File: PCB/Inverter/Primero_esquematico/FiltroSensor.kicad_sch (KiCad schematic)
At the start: 5 parts

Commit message: Termine el circuito de corriente
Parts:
- added C80: 2.2nF, symbol Device:C
- added C82, C83, C84: 300pF, symbol Device:C
- added R142, R143, R144: 100, symbol Device:R
- added R145, R146, R153: 5k1, symbol Device:R
- added U2: TLV9004QDRQ1, Package_SO:SOIC-14_3.9x8.7mm_P1.27mm, symbol Amplifier_Operational:TLV9004xRUCR
- C78: value 1nF -> 2.2nF
- C79: value 10n -> 2.2nF
- R138: value 15k -> 10k
- R139: value 51 -> 10k
- R140: value 100 -> 10k
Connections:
- net GND: now also R139.2, C80.1, C82.1, C83.1, C84.1, U2.10 (V-)
- removed net Sensor_In: C78.2, R138.1, R139.1
- removed net Sensor_Out: C79.2, R139.2, R140.1
- new net: R143.2, U2.5 (-), U2.6
- new net: R144.2, U2.7, U2.8 (-)
- new net: R142.2, U2.1 (-), U2.14
- new net: R140.1, R153.1, U2.9 (+)
- new net: R138.1, R145.1, U2.2 (+)
- new net: R139.1, R146.1, U2.4 (+)
- new net +3.3V: U2.3 (V+)
- new net Sensor_In_1: C78.2, R145.2
- new net Sensor_In_2: C79.2, R146.2
- new net Sensor_In_3: C80.2, R153.2
- new net Sensor_Out_1: C82.2, R142.1
- new net Sensor_Out_2: C83.2, R143.1
- new net Sensor_Out_3: C84.2, R144.1
- no-connect marks 0 -> 3
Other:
- note added: "CL<2.2 nF Rl>10k Ohms"
- moved on the sheet: C78, R138

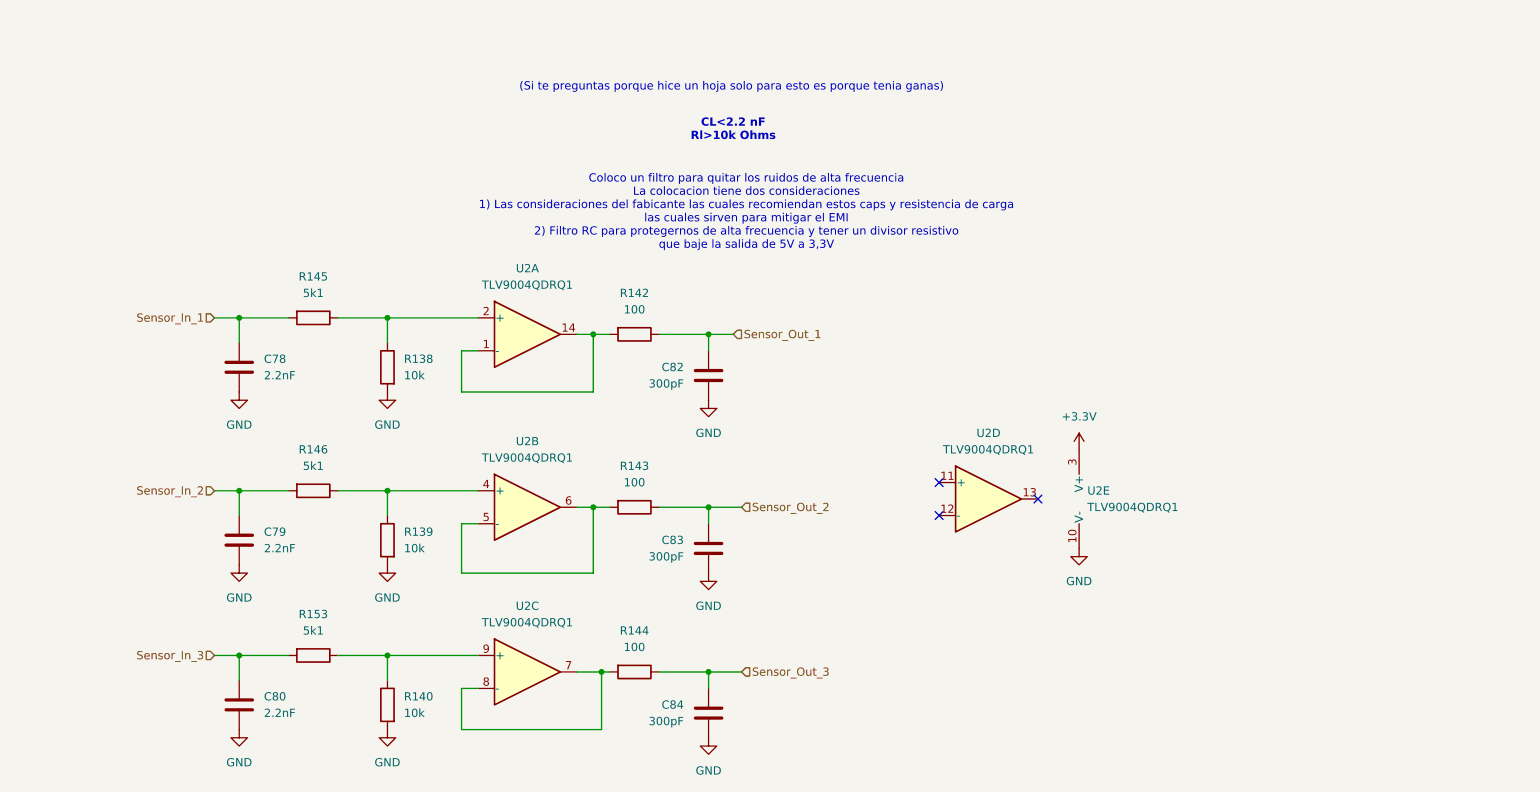
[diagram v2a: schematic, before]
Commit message: Coloque filtros y sensores
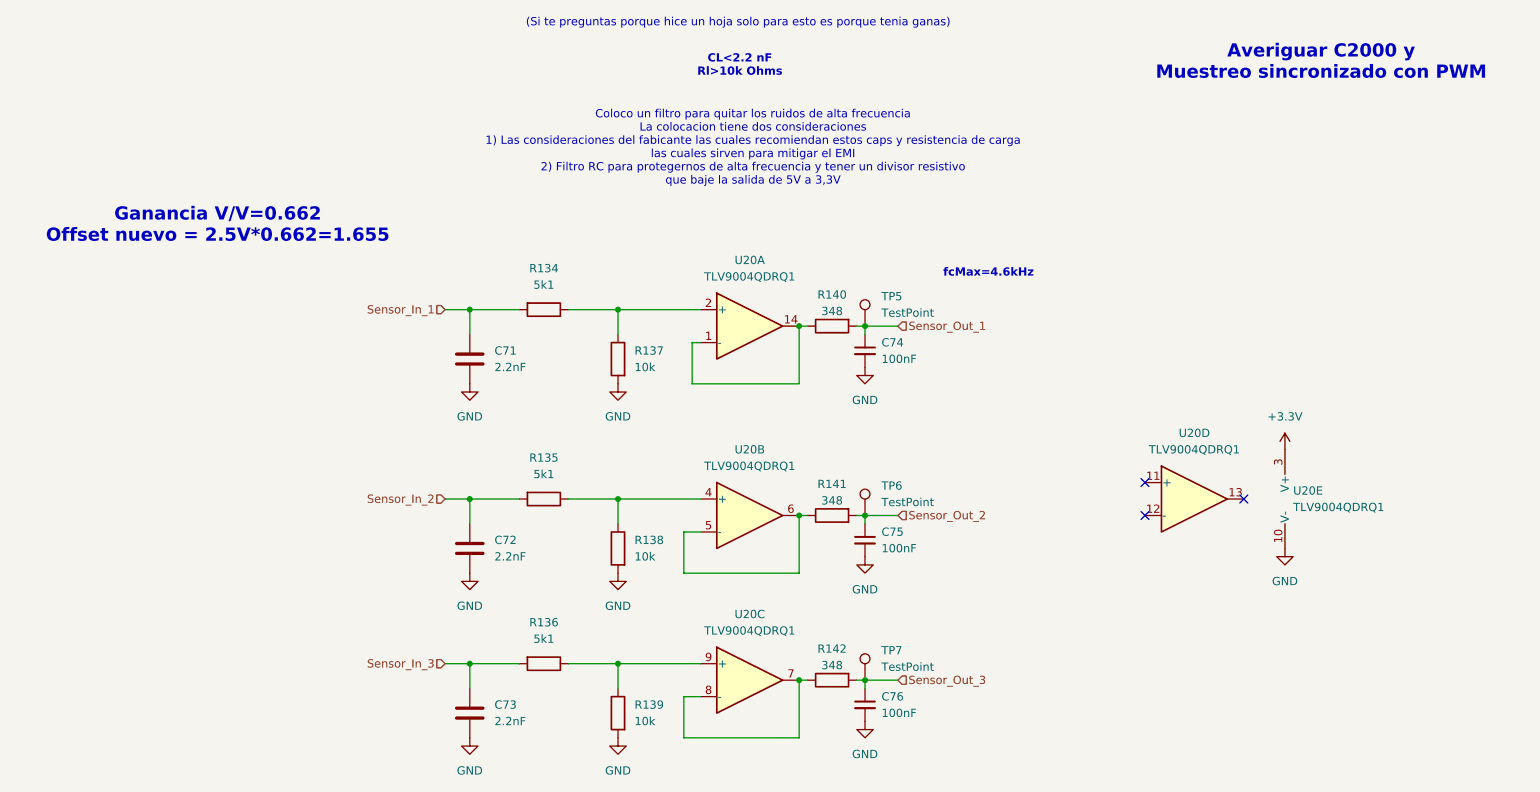
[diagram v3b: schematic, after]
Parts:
- removed C82, C83, C84: 300pF, symbol Device:C
- removed R143, R144: 100, symbol Device:R
- added C74, C75, C76: 100nF, symbol Device:C_Small
- added R140, R141: 348, symbol Device:R
- added TP5, TP6, TP7: TestPoint, symbol Connector:TestPoint
- R142: value 100 -> 348
- renumbered C78 to C71, C79 to C72, C80 to C73, R145 to R134, R146 to R135, R153 to R136, R138 to R137, R139 to R138, R140 to R139, U2 to U20
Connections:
- net GND: now also C74.2, C75.2, C76.2
- net Sensor_Out_1: now also C74.1, R140.2, TP5.1; no longer R142.1
- net Sensor_Out_2: now also C75.1, R141.2, TP6.1
- net Sensor_Out_3: now also R142.2, C76.1, TP7.1
- net at U20.5 (-), U20.6: now also R141.1
- net at U20.7, U20.8 (-): now also R142.1
- net at U20.1 (-), U20.14: now also R140.1; no longer R142.2
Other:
- note added: "Averiguar C2000 y Muestreo sincronizado con PWM"
- note added: "Ganancia V/V=0.662 Offset nuevo = 2.5V*0.662=1.655"
- note added: "fcMax=4.6kHz"
- moved on the sheet: C71, C72, C73, R134, R135, R136, R137, R138, R139, U20A, U20B, U20C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

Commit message: Esquematico practicamente terminado
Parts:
- C71, C72, C73, C74, C75, C76: footprint (none) -> Capacitor_SMD:C_0603_1608Metric
- R134, R135, R136, R137, R138, R139, R140, R141, R142: footprint (none) -> Resistor_SMD:R_0402_1005Metric
- TP5, TP6, TP7: footprint (none) -> TestPoint:TestPoint_Pad_D2.0mm
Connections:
- net +3.3V renamed +3.3VA
- net GND renamed GND1

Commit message: Un par de cosas q corregi del ERC pero sigue mal
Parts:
- U20: footprint Package_SO:SOIC-14_3.9x8.7mm_P1.27mm -> Package_DFN_QFN:Texas_S-PX2QFN-14
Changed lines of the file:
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@@
 			)
 		)
-		(property "Description" "-- valores mixtos --"
+		(property "Description" "Resistor"
 			(at 129.54 133.35 0)
 			(hide yes)
@@
 			)
 		)
-		(property "Description" "-- valores mixtos --"
+		(property "Description" "Resistor"
 			(at 129.54 78.74 0)
 			(hide yes)
@@
 			)
 		)
-		(property "Description" "-- valores mixtos --"
+		(property "Description" "Resistor"
 			(at 129.54 107.95 0)
 			(hide yes)
@@
 			)
 		)
-		(property "Footprint" "Package_SO:SOIC-14_3.9x8.7mm_P1.27mm"
+		(property "Footprint" "Package_DFN_QFN:Texas_S-PX2QFN-14"
 			(at 149.86 73.66 0)
 			(hide yes)
@@
 			)
 		)
-		(property "Datasheet" "https://www.ti.com/lit/ds/symlink/tlv9002-q1.pdf"
+		(property "Datasheet" "http://www.ti.com/lit/ds/symlink/tlv9004.pdf"
 			(at 151.13 68.58 0)
 			(hide yes)
@@
 			)
 		)
-		(property "Description" "-- valores mixtos --"
+		(property "Description" "Low-Power, Quad-Operational Amplifiers, Texas S-PX2QFN-14"
 			(at 149.86 73.66 0)
 			(hide yes)
@@
 			)
 		)
-		(property "Footprint" "Package_SO:SOIC-14_3.9x8.7mm_P1.27mm"
+		(property "Footprint" "Package_DFN_QFN:Texas_S-PX2QFN-14"
 			(at 149.86 102.87 0)
 			(hide yes)
@@
 			)
 		)
-		(property "Datasheet" "https://www.ti.com/lit/ds/symlink/tlv9002-q1.pdf"
+		(property "Datasheet" "http://www.ti.com/lit/ds/symlink/tlv9004.pdf"
 			(at 151.13 97.79 0)
 			(hide yes)
@@
 			)
 		)
-		(property "Description" "-- valores mixtos --"
+		(property "Description" "Low-Power, Quad-Operational Amplifiers, Texas S-PX2QFN-14"
 			(at 149.86 102.87 0)
 			(hide yes)
@@
 			)
 		)
-		(property "Footprint" "Package_SO:SOIC-14_3.9x8.7mm_P1.27mm"
+		(property "Footprint" "Package_DFN_QFN:Texas_S-PX2QFN-14"
 			(at 149.86 128.27 0)
 			(hide yes)
@@
 			)
 		)
-		(property "Datasheet" "https://www.ti.com/lit/ds/symlink/tlv9002-q1.pdf"
+		(property "Datasheet" "http://www.ti.com/lit/ds/symlink/tlv9004.pdf"
 			(at 151.13 123.19 0)
 			(hide yes)
@@
 			)
 		)
-		(property "Description" "-- valores mixtos --"
+		(property "Description" "Low-Power, Quad-Operational Amplifiers, Texas S-PX2QFN-14"
 			(at 149.86 128.27 0)
 			(hide yes)
@@
 			)
 		)
-		(property "Footprint" "Package_SO:SOIC-14_3.9x8.7mm_P1.27mm"
+		(property "Footprint" "Package_DFN_QFN:Texas_S-PX2QFN-14"
 			(at 234.95 100.33 0)
 			(hide yes)
@@
 			)
 		)
-		(property "Datasheet" "https://www.ti.com/lit/ds/symlink/tlv9002-q1.pdf"
+		(property "Datasheet" "http://www.ti.com/lit/ds/symlink/tlv9004.pdf"
 			(at 236.22 95.25 0)
 			(hide yes)
@@
 			)
 		)
-		(property "Description" "-- valores mixtos --"
+		(property "Description" "Low-Power, Quad-Operational Amplifiers, Texas S-PX2QFN-14"
 			(at 234.95 100.33 0)
 			(hide yes)
@@
 			)
 		)
-		(property "Footprint" "Package_SO:SOIC-14_3.9x8.7mm_P1.27mm"
+		(property "Footprint" "Package_DFN_QFN:Texas_S-PX2QFN-14"
 			(at 218.44 100.33 0)
 			(hide yes)
@@
 			)
 		)
-		(property "Datasheet" "https://www.ti.com/lit/ds/symlink/tlv9002-q1.pdf"
+		(property "Datasheet" "http://www.ti.com/lit/ds/symlink/tlv9004.pdf"
 			(at 219.71 95.25 0)
 			(hide yes)
@@
 			)
 		)
-		(property "Description" "-- valores mixtos --"
+		(property "Description" "Low-Power, Quad-Operational Amplifiers, Texas S-PX2QFN-14"
 			(at 218.44 100.33 0)
 			(hide yes)

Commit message: correcciones
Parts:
- TP45: renamed from TP5; footprint TestPoint:TestPoint_Pad_D2.0mm -> TestPoint:TestPoint_Pad_D1.0mm
- TP46: renamed from TP6; footprint TestPoint:TestPoint_Pad_D2.0mm -> TestPoint:TestPoint_Pad_D1.0mm
- TP47: renamed from TP7; footprint TestPoint:TestPoint_Pad_D2.0mm -> TestPoint:TestPoint_Pad_D1.0mm
- renumbered C71 to C142, C72 to C143, C73 to C144, C74 to C145, C75 to C146, C76 to C147, R134 to R202, R135 to R203, R136 to R204, R137 to R205, R138 to R206, R139 to R207, R140 to R208, R141 to R209, R142 to R210, U20 to U37

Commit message: Algunos cambios
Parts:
- added C152: 100nF, Capacitor_SMD:C_0603_1608Metric, symbol Device:C
- C142, C143, C144, C145, C146, C147: footprint Capacitor_SMD:C_0603_1608Metric -> Capacitor_SMD:C_0402_1005Metric
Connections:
- net GND1: now also C152.1
- net +3.3VA renamed +3.3V_analog
- net +3.3V_analog: now also C152.2

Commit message: Corregi cosas de la placa
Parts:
- renumbered C142 to C162, C143 to C163, C144 to C164, C145 to C165, C146 to C166, C147 to C167, C152 to C168, U37 to U36
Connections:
- net GND1 renamed GND
